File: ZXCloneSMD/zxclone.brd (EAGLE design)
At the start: 31.8 x 20.3 mm, 18 parts, among them IC1 TLC272D

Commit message: On the way to a second proto board
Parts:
- added R8: TRIMPOT-2, SparkFun-Electromechanical:TRIMPOT_TC33
- C1: device resistor:E2,5-7 -> rcl:CT7343
- R1, R2, R3, R4, R5, R6: device resistor:R0805 -> resistor:R0402
- moved R4 13.1 mm to (16.5, 3.81), turned to 180 degrees
- moved R7 11.2 mm to (24.8, 15.4), turned to 180 degrees
- moved R3 10.9 mm to (16.5, 5.08), turned to 180 degrees
- moved R5 8.98 mm to (21.6, 3.81), turned to 180 degrees
- moved C3 5.72 mm to (14.2, 4.45)
- moved R1 4.02 mm to (19.1, 3.81), turned to 180 degrees
- moved C1 3.81 mm to (17.8, 16.5)
- moved R2 3.81 mm to (19.1, 5.08), turned to 0 degrees
- moved R6 3.81 mm to (21.6, 5.08), turned to 0 degrees
- moved C2 1.27 mm to (10.2, 3.81), turned to 180 degrees
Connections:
- new net N$6: R5.2, R8.1
- net GND: now also U$1.2; no longer U$1.1
- net N$1: now also R8.2; no longer R5.2
- net N$7: now also U$1.1; no longer U$1.2
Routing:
- net N$3: track 15.4 -> 44.6 mm
- net VCC: track 31.0 -> 11.3 mm
- net N$7: track 10.5 -> 28.9 mm
- net N$1: track 43.0 -> 26.8 mm
- net GND: track 61.8 -> 51.3 mm, vias 3 -> 1
- net SIG: track 51.3 -> 42.5 mm, vias 0 -> 1
- net N$6: track 0.00 -> 7.33 mm
- net N$2: track 13.2 -> 16.5 mm
- net N$5: track 13.2 -> 10.3 mm, vias 2 -> 3
- net N$4: track 12.2 -> 11.9 mm, vias 0 -> 2
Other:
- board text added: "20130630r02"
- board text removed: "100k"
- board text removed: "1k"
- board text removed: "20130612r01"
- board text removed: "22R"
- board text removed: "22k"
- board text removed: "22uF"
- board text removed: "470uF"
- board text removed: "68k"

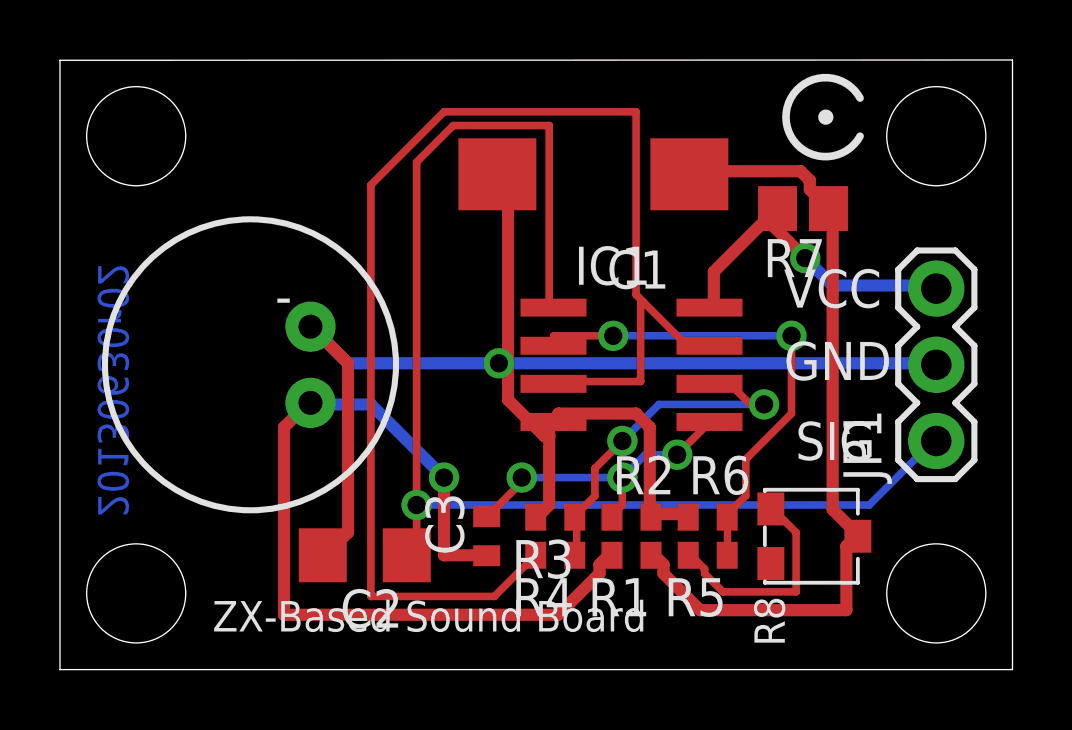
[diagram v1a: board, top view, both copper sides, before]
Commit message: Working revision with LED and trimpot
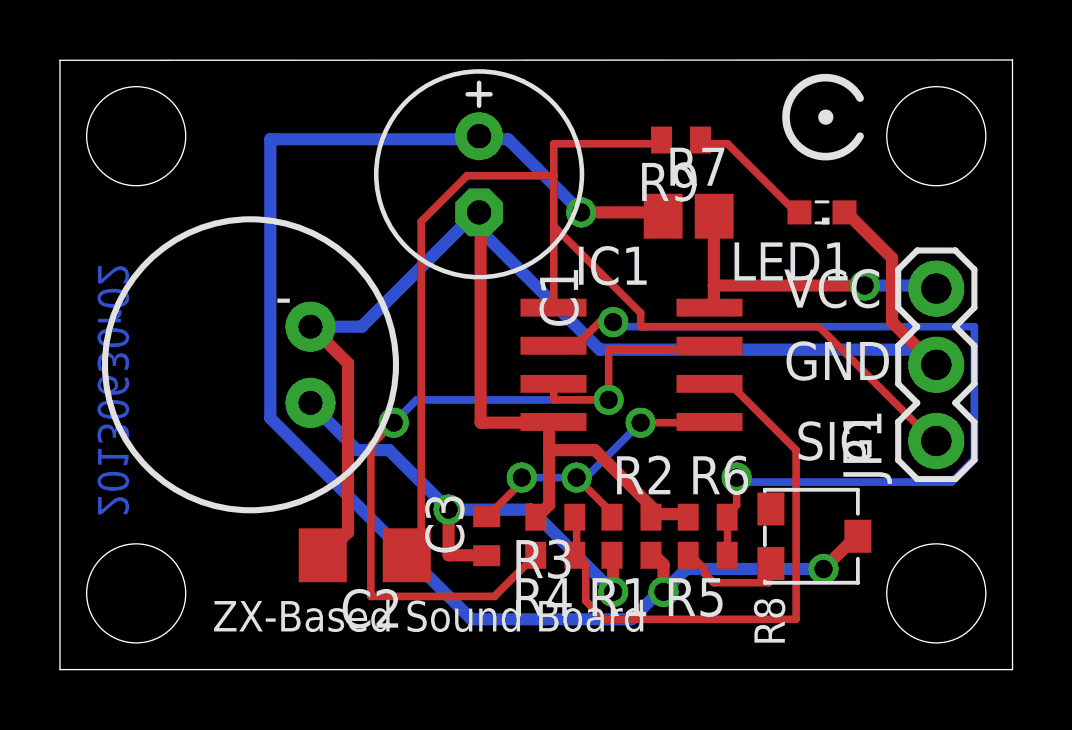
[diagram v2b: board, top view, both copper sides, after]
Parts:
- added LED1: (no value), led:SML0603
- added R9: 1k, resistor:R0402
- C1: device rcl:CT7343 -> resistor:E2,5-7
- R5: value 68k -> 30k
- R8: value TRIMPOT-2 -> TRIMPOT 25K
- moved R7 3.82 mm to (21.0, 15.1), turned to 0 degrees
- moved C1 3.81 mm to (14.0, 16.5), turned to 270 degrees
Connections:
- new net N$8: LED1.A, R9.1
- net GND: now also LED1.C
- net N$6: now also R8.3; no longer R8.1
- net SIG: now also R9.2
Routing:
- net N$1: track 26.8 -> 48.5 mm, vias 0 -> 3
- net N$3: track 44.6 -> 27.2 mm, vias 0 -> 2
- net N$2: track 16.5 -> 29.9 mm
- net N$7: track 28.9 -> 16.8 mm, vias 1 -> 2
- net N$4: track 11.9 -> 19.7 mm, vias 2 -> 0
- net GND: track 51.3 -> 58.9 mm, vias 1 -> 0
- net N$8: track 0.00 -> 4.30 mm
- net N$6: track 7.33 -> 3.84 mm
- net SIG: track 42.5 -> 41.5 mm, vias 1 -> 0
- net VCC: track 11.3 -> 10.6 mm
